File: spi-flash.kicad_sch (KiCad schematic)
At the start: 53 parts, among them J23 DM3AT-SF-PEJM5, U12 MT25QL256ABA1EW7-0SIT, U13 MT25QL256ABA1EW7-0SIT, U14 MT25QL256ABA1EW7-0SIT

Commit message: Bump revision to 1.0.0. Update name on schematic and PCB sheets
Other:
- title: K410T devboard -> Kintex 410T devboard

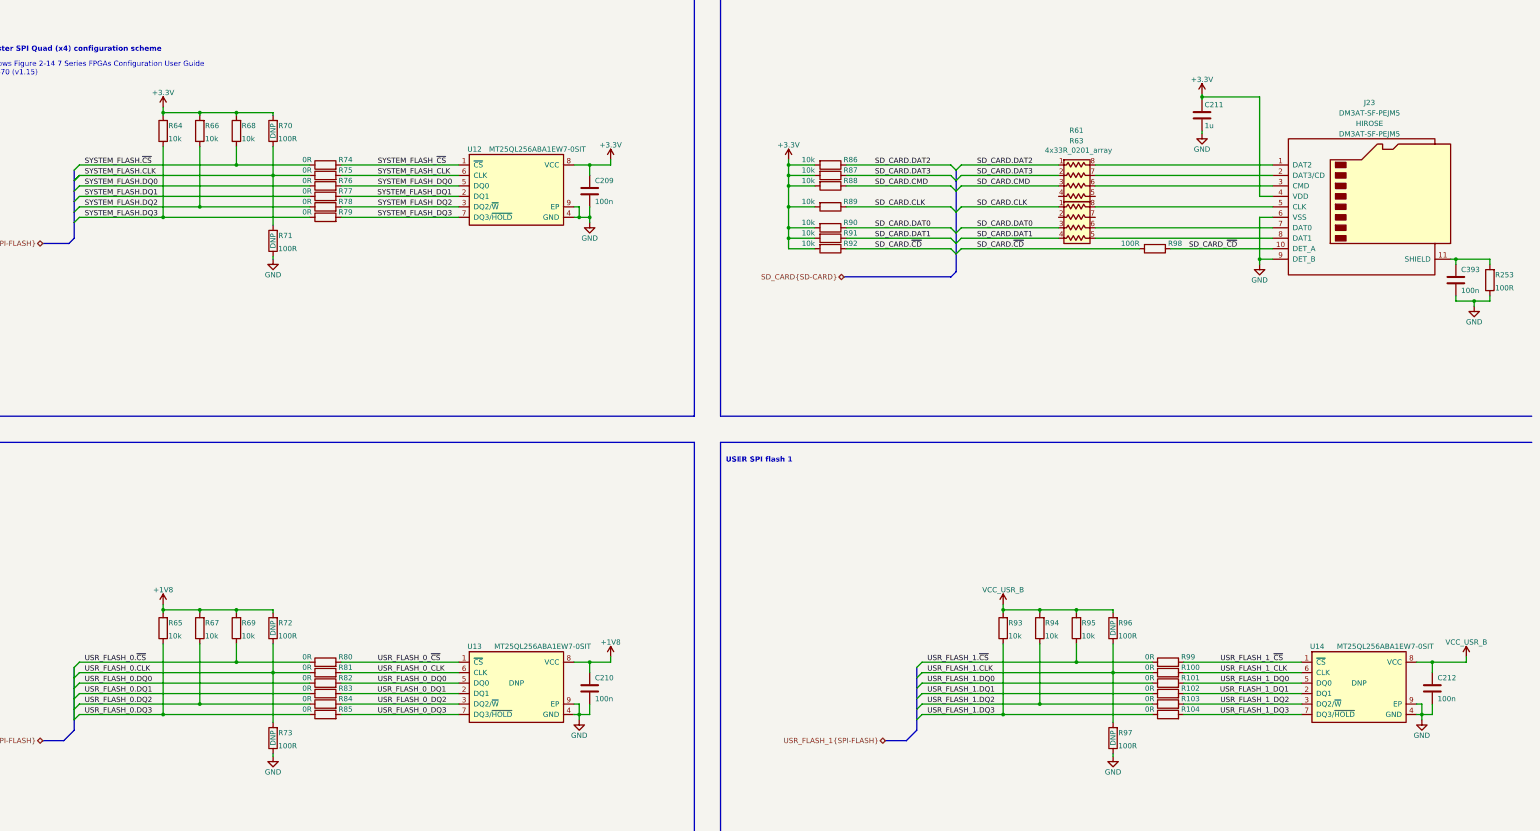
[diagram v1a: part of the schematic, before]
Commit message: Introduce component standardization
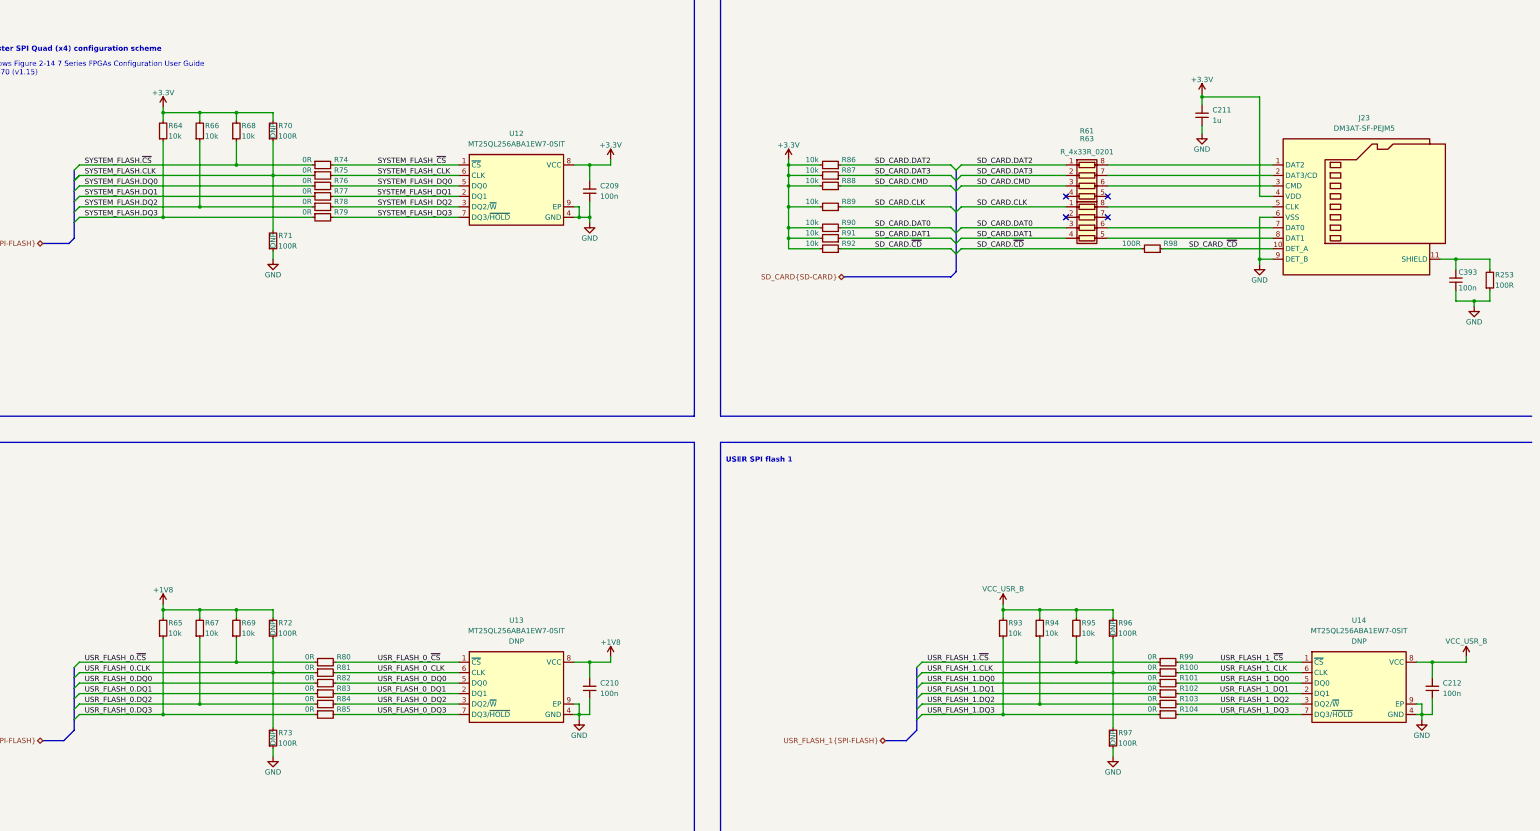
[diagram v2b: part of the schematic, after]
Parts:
- C209, C210, C212, C393: footprint K410T-devboard-footprints:0402-cap -> K410T-devboard-footprints:C_0402_1005Metric; Author (none) -> Antmicro; Dielectric (none) -> X5R; License (none) -> Apache-2.0; Voltage (none) -> 50V
- C211: footprint K410T-devboard-footprints:0402-cap -> K410T-devboard-footprints:C_0402_1005Metric; Author (none) -> Antmicro; License (none) -> Apache-2.0
- J23: Author (none) -> Antmicro; License (none) -> Apache-2.0; Manufacturer HIROSE -> Hirose
- R100, R101, R102, R103, R104, R74, R75, R76, R77, R78, R79, R80, R81, R82, R83, R84, R85, R99: footprint K410T-devboard-footprints:0402-res -> K410T-devboard-footprints:R_0402_1005Metric; Author (none) -> Antmicro; Current (none) -> 1A; License (none) -> Apache-2.0; Manufacturer PANASONIC -> Panasonic
- R253, R70, R71, R72, R73, R96, R97, R98: footprint K410T-devboard-footprints:0402-res -> K410T-devboard-footprints:R_0402_1005Metric; Author (none) -> Antmicro; License (none) -> Apache-2.0; Manufacturer BOURNS -> Bourns; Tolerance (none) -> 1%
- R61, R63: value 4x33R_0201_array -> R_4x33R_0201_array; footprint K410T-devboard-footprints:EXB18V -> K410T-devboard-footprints:R_Array_4x0201_Panasonic_EXB18V; symbol K410T-devboard:4x33R_0201_array -> K410T-devboard:R_4x33R_0201_array; Author (none) -> Antmicro; License (none) -> Apache-2.0; Val (none) -> R_4x33R_0201
- R64, R65, R66, R67, R68, R69, R86, R87, R88, R89, R90, R91, R92, R93, R94, R95: footprint K410T-devboard-footprints:0402-res -> K410T-devboard-footprints:R_0402_1005Metric; Author (none) -> Antmicro; License (none) -> Apache-2.0; MPN CRCW040210K0FKEDHP -> CR0402-FX-1002GLF; Manufacturer VISHAY -> Bourns; Tolerance (none) -> 1%
- U12, U13, U14: footprint K410T-devboard-footprints:WSON8x6_WSON6x5_dual -> K410T-devboard-footprints:WDFN-8-1EP_6x5mm_P1.27mm_EP3.4x4mm; Author (none) -> Antmicro; License (none) -> Apache-2.0
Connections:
- net +1V8: now also C210.2; no longer C210.1
- net +3V3: now also C209.2, C211.2; no longer C209.1, C211.1
- net GND: now also C209.1, C210.1, C211.1, C212.1, C393.1; no longer C209.2, C210.2, C211.2, C212.2, C393.2
- net VCC_USR_B: now also C212.2; no longer C212.1
- net at J23.11 (SHIELD), R253.2: now also C393.2; no longer C393.1
- no-connect marks 0 -> 4
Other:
- moved on the sheet: C209, C210, C211, C212, C393, R74, R75, R76, R77, R78, R79, R98

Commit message: [#55729] Fix DM3AT-SF-PEJM5
Save project as KiCad 7
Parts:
- J23: footprint K410T-devboard-footprints:MicroSD_DM3AT-SF-PEJM5 -> antmicro-footprints:MicroSD_DM3AT-SF-PEJM5; symbol K410T-devboard:DM3AT-SF-PEJM5 -> antmicroMemoryConnectorsPCCardSockets:DM3AT-SF-PEJM5; Manufacturer Hirose -> Hirose Electric

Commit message: [#55729] Fix batch of components Fix ftdi-ft4232h-56q-reel Fix maxim-integrated-max3421eetj Fix maxim-integrated-max16150aut-t Fix maxim-integrated-max1617amee-t Fix micron-mt25ql256aba1ew7-0sit
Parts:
- U12, U13, U14: footprint K410T-devboard-footprints:WDFN-8-1EP_6x5mm_P1.27mm_EP3.4x4mm -> antmicro-footprints:WDFN-8-1EP_6x5mm_P1.27mm_EP3.4x4mm; symbol K410T-devboard:MT25QL256ABA1EW7-0SIT -> antmicroMemory:MT25QL256ABA1EW7-0SIT; Manufacturer Micron -> Micron Technology
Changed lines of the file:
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@@
     (title "Kintex 410T devboard")
     (date "2023-02-01")
-    (rev "1.1.1")
+    (rev "1.1.1:14a15")
   )
   (junction (at 226.06 83.82) (diameter 0) (color 0 0 0 0)
@@
     )
   )
-  (symbol (lib_id "K410T-devboard:MT25QL256ABA1EW7-0SIT") (at 146.05 66.04 0) (unit 1)
+  (symbol (lib_id "antmicroMemory:MT25QL256ABA1EW7-0SIT") (at 146.05 66.04 0) (unit 1)
     (in_bom yes) (on_board yes) (dnp no) (fields_autoplaced)
     (property "Reference" "U12" (at 160.02 58.42 0)
@@
       (effects (font (size 1.27 1.27) (thickness 0.15)))
     )
-    (property "Footprint" "K410T-devboard-footprints:WDFN-8-1EP_6x5mm_P1.27mm_EP3.4x4mm" (at 187.96 73.66 0)
+    (property "Footprint" "antmicro-footprints:WDFN-8-1EP_6x5mm_P1.27mm_EP3.4x4mm" (at 187.96 73.66 0)
       (effects (font (size 1.27 1.27) (thickness 0.15)) (justify left bottom) hide)
     )
@@
       (effects (font (size 1.27 1.27) (thickness 0.15)) (justify left bottom) hide)
     )
-    (property "Manufacturer" "Micron" (at 187.96 81.28 0)
+    (property "Manufacturer" "Micron Technology" (at 187.96 81.28 0)
       (effects (font (size 1.27 1.27) (thickness 0.15)) (justify left bottom) hide)
     )
@@
     )
   )
-  (symbol (lib_id "K410T-devboard:MT25QL256ABA1EW7-0SIT") (at 350.52 186.69 0) (unit 1)
+  (symbol (lib_id "antmicroMemory:MT25QL256ABA1EW7-0SIT") (at 350.52 186.69 0) (unit 1)
     (in_bom yes) (on_board yes) (dnp no) (fields_autoplaced)
     (property "Reference" "U14" (at 364.49 176.53 0)
@@
       (effects (font (size 1.27 1.27) (thickness 0.15)))
     )
-    (property "Footprint" "K410T-devboard-footprints:WDFN-8-1EP_6x5mm_P1.27mm_EP3.4x4mm" (at 392.43 194.31 0)
+    (property "Footprint" "antmicro-footprints:WDFN-8-1EP_6x5mm_P1.27mm_EP3.4x4mm" (at 392.43 194.31 0)
       (effects (font (size 1.27 1.27) (thickness 0.15)) (justify left bottom) hide)
     )
@@
       (effects (font (size 1.27 1.27) (thickness 0.15)) (justify left bottom) hide)
     )
-    (property "Manufacturer" "Micron" (at 392.43 201.93 0)
+    (property "Manufacturer" "Micron Technology" (at 392.43 201.93 0)
       (effects (font (size 1.27 1.27) (thickness 0.15)) (justify left bottom) hide)
     )
@@
     )
   )
-  (symbol (lib_id "K410T-devboard:MT25QL256ABA1EW7-0SIT") (at 146.05 186.69 0) (unit 1)
+  (symbol (lib_id "antmicroMemory:MT25QL256ABA1EW7-0SIT") (at 146.05 186.69 0) (unit 1)
     (in_bom yes) (on_board yes) (dnp no) (fields_autoplaced)
     (property "Reference" "U13" (at 160.02 176.53 0)
@@
       (effects (font (size 1.27 1.27) (thickness 0.15)))
     )
-    (property "Footprint" "K410T-devboard-footprints:WDFN-8-1EP_6x5mm_P1.27mm_EP3.4x4mm" (at 187.96 194.31 0)
+    (property "Footprint" "antmicro-footprints:WDFN-8-1EP_6x5mm_P1.27mm_EP3.4x4mm" (at 187.96 194.31 0)
       (effects (font (size 1.27 1.27) (thickness 0.15)) (justify left bottom) hide)
     )
@@
       (effects (font (size 1.27 1.27) (thickness 0.15)) (justify left bottom) hide)
     )
-    (property "Manufacturer" "Micron" (at 187.96 201.93 0)
+    (property "Manufacturer" "Micron Technology" (at 187.96 201.93 0)
       (effects (font (size 1.27 1.27) (thickness 0.15)) (justify left bottom) hide)
     )

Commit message: [#55729] Run loclib
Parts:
- J23: footprint antmicro-footprints:MicroSD_DM3AT-SF-PEJM5 -> K410T-devboard-footprints:MicroSD_DM3AT-SF-PEJM5; symbol antmicroMemoryConnectorsPCCardSockets:DM3AT-SF-PEJM5 -> K410T-devboard:DM3AT-SF-PEJM5
- U12, U13, U14: footprint antmicro-footprints:WDFN-8-1EP_6x5mm_P1.27mm_EP3.4x4mm -> K410T-devboard-footprints:WDFN-8-1EP_6x5mm_P1.27mm_EP3.4x4mm; symbol antmicroMemory:MT25QL256ABA1EW7-0SIT -> K410T-devboard:MT25QL256ABA1EW7-0SIT
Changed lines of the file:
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@@
     )
   )
-  (symbol (lib_id "antmicroMemory:MT25QL256ABA1EW7-0SIT") (at 146.05 66.04 0) (unit 1)
+  (symbol (lib_id "K410T-devboard:MT25QL256ABA1EW7-0SIT") (at 146.05 66.04 0) (unit 1)
     (in_bom yes) (on_board yes) (dnp no) (fields_autoplaced)
     (property "Reference" "U12" (at 160.02 58.42 0)
@@
       (effects (font (size 1.27 1.27) (thickness 0.15)))
     )
-    (property "Footprint" "antmicro-footprints:WDFN-8-1EP_6x5mm_P1.27mm_EP3.4x4mm" (at 187.96 73.66 0)
+    (property "Footprint" "K410T-devboard-footprints:WDFN-8-1EP_6x5mm_P1.27mm_EP3.4x4mm" (at 187.96 73.66 0)
       (effects (font (size 1.27 1.27) (thickness 0.15)) (justify left bottom) hide)
     )
@@
     )
   )
-  (symbol (lib_id "antmicroMemory:MT25QL256ABA1EW7-0SIT") (at 350.52 186.69 0) (unit 1)
+  (symbol (lib_id "K410T-devboard:MT25QL256ABA1EW7-0SIT") (at 350.52 186.69 0) (unit 1)
     (in_bom yes) (on_board yes) (dnp no) (fields_autoplaced)
     (property "Reference" "U14" (at 364.49 176.53 0)
@@
       (effects (font (size 1.27 1.27) (thickness 0.15)))
     )
-    (property "Footprint" "antmicro-footprints:WDFN-8-1EP_6x5mm_P1.27mm_EP3.4x4mm" (at 392.43 194.31 0)
+    (property "Footprint" "K410T-devboard-footprints:WDFN-8-1EP_6x5mm_P1.27mm_EP3.4x4mm" (at 392.43 194.31 0)
       (effects (font (size 1.27 1.27) (thickness 0.15)) (justify left bottom) hide)
     )
@@
     )
   )
-  (symbol (lib_id "antmicroMemoryConnectorsPCCardSockets:DM3AT-SF-PEJM5") (at 343.535 66.04 0) (unit 1)
+  (symbol (lib_id "K410T-devboard:DM3AT-SF-PEJM5") (at 343.535 66.04 0) (unit 1)
     (in_bom yes) (on_board yes) (dnp no) (fields_autoplaced)
     (property "Reference" "J23" (at 365.76 54.61 0)
@@
       (effects (font (size 1.27 1.27) (thickness 0.15)))
     )
-    (property "Footprint" "antmicro-footprints:MicroSD_DM3AT-SF-PEJM5" (at 400.685 71.12 0)
+    (property "Footprint" "K410T-devboard-footprints:MicroSD_DM3AT-SF-PEJM5" (at 400.685 71.12 0)
       (effects (font (size 1.27 1.27) (thickness 0.15)) (justify left bottom) hide)
     )
@@
     )
   )
-  (symbol (lib_id "antmicroMemory:MT25QL256ABA1EW7-0SIT") (at 146.05 186.69 0) (unit 1)
+  (symbol (lib_id "K410T-devboard:MT25QL256ABA1EW7-0SIT") (at 146.05 186.69 0) (unit 1)
     (in_bom yes) (on_board yes) (dnp no) (fields_autoplaced)
     (property "Reference" "U13" (at 160.02 176.53 0)
@@
       (effects (font (size 1.27 1.27) (thickness 0.15)))
     )
-    (property "Footprint" "antmicro-footprints:WDFN-8-1EP_6x5mm_P1.27mm_EP3.4x4mm" (at 187.96 194.31 0)
-      (effects (font (size 1.27 1.27) (thickness 0.15)) (justify left bottom) hide)
-    )
+    (property "Footprint" "K410T-devboard-footprints:WDFN-8-1EP_6x5mm_P1.27mm_EP3.4x4mm" (at 187.96 194.31 0)
+      (effects (font (size 1.27 1.27) (thickness 0.15)) (justify left bottom) hide)
+    )

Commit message: [#55729] Globlib; Clean DNP; Realign to grid
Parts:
- C209, C210, C212, C393: footprint K410T-devboard-footprints:C_0402_1005Metric -> antmicro-footprints:C_0402_1005Metric; symbol K410T-devboard:C_100n_0402 -> antmicroCapacitors0402:C_100n_0402
- C211: footprint K410T-devboard-footprints:C_0402_1005Metric -> antmicro-footprints:C_0402_1005Metric; symbol K410T-devboard:C_1u_0402 -> antmicroCapacitors0402:C_1u_0402
- J23: footprint K410T-devboard-footprints:MicroSD_DM3AT-SF-PEJM5 -> antmicro-footprints:MicroSD_DM3AT-SF-PEJM5; symbol K410T-devboard:DM3AT-SF-PEJM5 -> antmicroMemoryConnectorsPCCardSockets:DM3AT-SF-PEJM5
- R100, R101, R102, R103, R104, R74, R75, R76, R77, R78, R79, R80, R81, R82, R83, R84, R85, R99: footprint K410T-devboard-footprints:R_0402_1005Metric -> antmicro-footprints:R_0402_1005Metric; symbol K410T-devboard:R_0R_0402 -> antmicroResistors0402:R_0R_0402
- R253, R98: footprint K410T-devboard-footprints:R_0402_1005Metric -> antmicro-footprints:R_0402_1005Metric; symbol K410T-devboard:R_100R_0402 -> antmicroResistors0402:R_100R_0402
- R61, R63: footprint K410T-devboard-footprints:R_Array_4x0201_Panasonic_EXB18V -> antmicro-footprints:R_Array_4x0201_Panasonic_EXB18V; symbol K410T-devboard:R_4x33R_0201_array -> antmicroResistorNetworksArrays:R_4x33R_0201_array
- R64, R65, R66, R67, R68, R69, R86, R87, R88, R89, R90, R91, R92, R93, R94, R95: footprint K410T-devboard-footprints:R_0402_1005Metric -> antmicro-footprints:R_0402_1005Metric; symbol K410T-devboard:R_10k_0402 -> antmicroResistors0402:R_10k_0402
- R70, R71, R72, R73, R96, R97: footprint K410T-devboard-footprints:R_0402_1005Metric -> antmicro-footprints:R_0402_1005Metric; symbol K410T-devboard:R_100R_0402 -> antmicroResistors0402:R_100R_0402; now not fitted; now left out of the parts list
- U12: footprint K410T-devboard-footprints:WDFN-8-1EP_6x5mm_P1.27mm_EP3.4x4mm -> antmicro-footprints:WDFN-8-1EP_6x5mm_P1.27mm_EP3.4x4mm; symbol K410T-devboard:MT25QL256ABA1EW7-0SIT -> antmicroMemory:MT25QL256ABA1EW7-0SIT
- U13, U14: footprint K410T-devboard-footprints:WDFN-8-1EP_6x5mm_P1.27mm_EP3.4x4mm -> antmicro-footprints:WDFN-8-1EP_6x5mm_P1.27mm_EP3.4x4mm; symbol K410T-devboard:MT25QL256ABA1EW7-0SIT -> antmicroMemory:MT25QL256ABA1EW7-0SIT; now not fitted; now left out of the parts list
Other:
- moved on the sheet: C211, C393, J23, R100, R101, R102, R103, R104, R64, R65, R66, R67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
